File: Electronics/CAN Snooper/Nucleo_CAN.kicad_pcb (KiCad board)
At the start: 2 copper layers, 54.6 x 50.8 mm, 38 parts, among them J1 Car Power, J2 CAN Bus, SW1 Reset, T1 12V Iso Test, T10 CAN L Test, T11 CAN Output GND Test, T2 5V Iso Test, T3 9V Test, T4 3.3V Test, T5 CAN PwrSense Test, T6 CAN Tx Test, T7 CAN Rx Test, T8 CAN Input GND Test, T9 CAN H Test, U1 PDS1-S12-S9-M, U2 MCP1702T-5002E/CB, U3 Nucleo_L432KC, U4 ADM3054

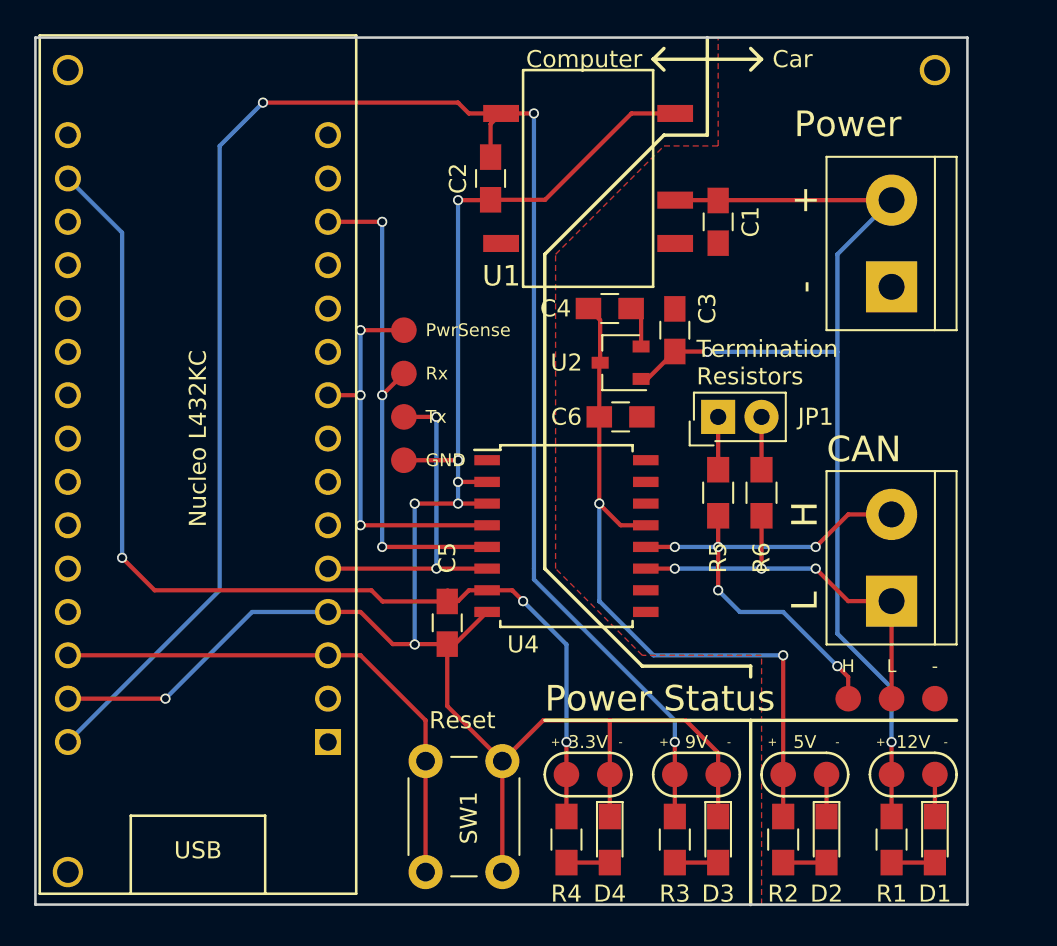
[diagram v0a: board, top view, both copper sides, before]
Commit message: CAN Snooper: PCB: Rerouted for new connectors; bumped PCB rev.
I reimported the netlist into the PCB and rerouted the car side of the
board to accommodate the new connectors. I also added a ground plane
to the computer side of the board and rerouted its traces to
accommodate said plane.
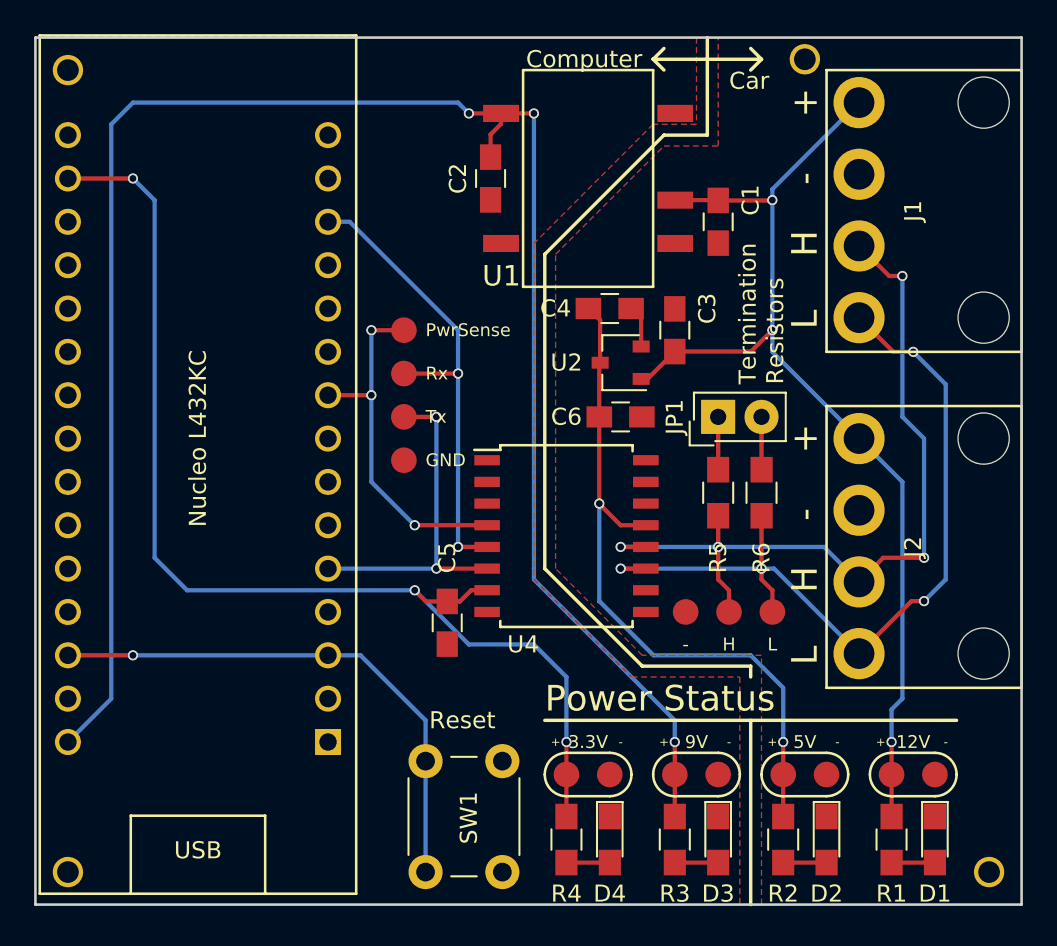
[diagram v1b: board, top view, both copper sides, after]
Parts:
- added REF**: MountingHole, Custom:MountingHole, F.Cu at (212.7, 100.3)
- J1: value Car Power -> CAN_In; footprint Connectors_Terminal_Blocks:TerminalBlock_bornier-2_P5.08mm -> Custom:Molex-MiniFitJr-4-peg
- J2: value CAN Bus -> CAN_Out; footprint Connectors_Terminal_Blocks:TerminalBlock_bornier-2_P5.08mm -> Custom:Molex-MiniFitJr-4-peg
- moved T11 15.5 mm to (194.9, 85.1)
- moved J1 11.0 mm to (205.1, 55.2), turned to 0 degrees
- moved J2 9.71 mm to (205.1, 74.9), turned to 0 degrees
- moved T10 8.64 mm to (200.0, 85.1)
- moved T9 8.64 mm to (197.5, 85.1)
- moved REF** 7.65 mm to (201.9, 52.7)
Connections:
- J1 pad 1: GNDPWR -> +12V
- J1 pad 2: +12V -> GNDPWR
- J2 pad 1: /CAN_L -> +12V
- J2 pad 2: /CAN_H -> GNDPWR
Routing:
- net GND: track 116.7 -> 0.00 mm, vias 7 -> 0
- net /CAN_L: track 24.0 -> 48.4 mm, vias 3 -> 4
- net /CAN_H: track 30.5 -> 46.9 mm, vias 5 -> 4
- net GNDPWR: track 7.39 -> 2.47 mm
- net +9V: track 105.8 -> 110.2 mm
- net +3V3: track 63.0 -> 66.5 mm
- net /CAN_Rx: track 30.2 -> 27.8 mm, vias 3 -> 2
- net /CAN_PwrSense: track 23.3 -> 21.2 mm
- net +12V: track 63.6 -> 62.0 mm, vias 2 -> 3
- net +5VP: track 42.3 -> 41.2 mm
- net /RST: track 31.9 -> 31.4 mm, vias 0 -> 1
- added copper zone on F.Cu, net GND
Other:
- board size 54.6 x 50.8 mm -> 57.8 x 50.8 mm
- board text removed: "CAN"
- board text removed: "Power"

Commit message: CAN Snooper: PCB: Use nonplated M2 screw mounting holes
The previous mounting holes were a nonstandard size as far as I could
tell, so I replaced them with properly sized holes for M2 screws. I
also added circles in the Dwgs.User layer to indicate estimated screw
head size.

The components on the PCB may need to be moved around to make sure the
screw heads fit completely onto the PCB unobstructed.

Added three new footprints for mounting holes for metric screw sizes
M1.6, M1.8, and M2. Removed the old mounting hole footprint.
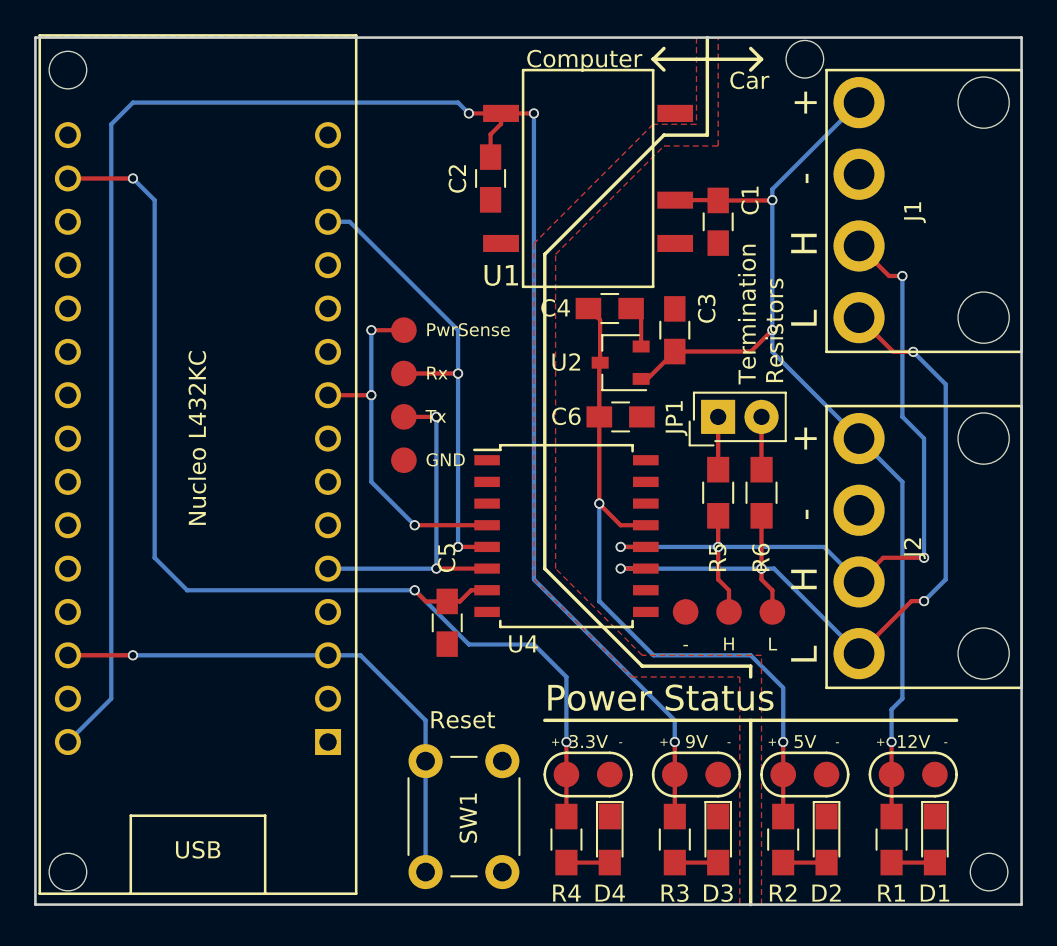
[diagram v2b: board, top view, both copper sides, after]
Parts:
- REF** (x4): footprint Custom:MountingHole -> Custom:MountingHole-M2-nonplated
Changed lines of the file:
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@@
     (links 71)
     (no_connects 0)
-    (area 156.769999 51.359999 211.530001 102.310001)
+    (area 148.689287 47.465 219.280001 104.077381)
     (thickness 1.6)
-    (drawings 53)
+    (drawings 57)
     (tracks 156)
     (zones 0)
@@
     (pad "" np_thru_hole circle (at 7.3 0) (size 3 3) (drill 3) (layers *.Cu))
   )
-  (module Custom:MountingHole (layer F.Cu)
-    (at 212.725 100.33)
-    (fp_text reference REF** (at 0 2.54) (layer F.SilkS) hide
-      (effects (font (size 1 1) (thickness 0.15)))
-    )
-    (fp_text value MountingHole (at 0 -2.54) (layer F.Fab)
-      (effects (font (size 1 1) (thickness 0.15)))
-    )
-    (pad "" thru_hole circle (at 0 0) (size 1.778 1.778) (drill 1.27) (layers *.Cu *.Mask))
-  )
   (module Connectors_Samtec:SL-102-X-XX_1x02 (layer F.Cu)
     (at 196.85 73.66 90)
@@
       (net 6 +3V3) (zone_connect 2))
   )
-  (module Custom:MountingHole (layer F.Cu)
-    (at 158.75 53.34)
-    (fp_text reference REF** (at 0 2.54) (layer F.SilkS) hide
-      (effects (font (size 1 1) (thickness 0.15)))
-    )
-    (fp_text value MountingHole (at 0 -2.54) (layer F.Fab)
-      (effects (font (size 1 1) (thickness 0.15)))
-    )
-    (pad "" thru_hole circle (at 0 0) (size 1.778 1.778) (drill 1.27) (layers *.Cu *.Mask))
-  )
-  (module Custom:MountingHole (layer F.Cu)
-    (at 158.75 100.33)
-    (fp_text reference REF** (at 0 2.54) (layer F.SilkS) hide
-      (effects (font (size 1 1) (thickness 0.15)))
-    )
-    (fp_text value MountingHole (at 0 -2.54) (layer F.Fab)
-      (effects (font (size 1 1) (thickness 0.15)))
-    )
-    (pad "" thru_hole circle (at 0 0) (size 1.778 1.778) (drill 1.27) (layers *.Cu *.Mask))
-  )
-  (module Custom:MountingHole (layer F.Cu)
-    (at 201.93 52.705)
-    (fp_text reference REF** (at 0 2.54) (layer F.SilkS) hide
-      (effects (font (size 1 1) (thickness 0.15)))
-    )
-    (fp_text value MountingHole (at 0 -2.54) (layer F.Fab)
-      (effects (font (size 1 1) (thickness 0.15)))
-    )
-    (pad "" thru_hole circle (at 0 0) (size 1.778 1.778) (drill 1.27) (layers *.Cu *.Mask))
-  )
   (module Custom:Molex-MiniFitJr-4-peg (layer F.Cu)
     (at 205.105 55.245)
@@
     (pad "" np_thru_hole circle (at 7.3 0) (size 3 3) (drill 3) (layers *.Cu))
   )
+  (module Custom:MountingHole-M2-nonplated (layer F.Cu)
+    (at 158.75 53.34)
+    (fp_text reference REF** (at 0 1.905) (layer F.SilkS) hide
+      (effects (font (size 1 1) (thickness 0.15)))
+    )
+    (fp_text value MountingHole (at 0 -1.905) (layer F.Fab)
+      (effects (font (size 1 1) (thickness 0.15)))
+    )
+    (pad "" np_thru_hole circle (at 0 0) (size 2.2 2.2) (drill 2.2) (layers *.Cu *.Mask))
+  )
+  (module Custom:MountingHole-M2-nonplated (layer F.Cu)
+    (at 158.75 100.33)
+    (fp_text reference REF** (at 0 1.905) (layer F.SilkS) hide
+      (effects (font (size 1 1) (thickness 0.15)))
+    )
+    (fp_text value MountingHole (at 0 -1.905) (layer F.Fab)
+      (effects (font (size 1 1) (thickness 0.15)))
+    )
+    (pad "" np_thru_hole circle (at 0 0) (size 2.2 2.2) (drill 2.2) (layers *.Cu *.Mask))
+  )
+  (module Custom:MountingHole-M2-nonplated (layer F.Cu)
+    (at 212.725 100.33)
+    (fp_text reference REF** (at 0 1.905) (layer F.SilkS) hide
+      (effects (font (size 1 1) (thickness 0.15)))
+    )
+    (fp_text value MountingHole (at 0 -1.905) (layer F.Fab)
+      (effects (font (size 1 1) (thickness 0.15)))
+    )
+    (pad "" np_thru_hole circle (at 0 0) (size 2.2 2.2) (drill 2.2) (layers *.Cu *.Mask))
+  )
+  (module Custom:MountingHole-M2-nonplated (layer F.Cu)
+    (at 201.93 52.705)
+    (fp_text reference REF** (at 0 1.905) (layer F.SilkS) hide
+      (effects (font (size 1 1) (thickness 0.15)))
+    )
+    (fp_text value MountingHole (at 0 -1.905) (layer F.Fab)
+      (effects (font (size 1 1) (thickness 0.15)))
+    )
+    (pad "" np_thru_hole circle (at 0 0) (size 2.2 2.2) (drill 2.2) (layers *.Cu *.Mask))
+  )
+  (gr_circle (center 201.93 52.705) (end 201.93 54.905) (layer Dwgs.User) (width 0.2))
+  (gr_circle (center 212.725 100.33) (end 212.725 102.53) (layer Dwgs.User) (width 0.2))
+  (gr_circle (center 158.75 100.33) (end 158.75 102.53) (layer Dwgs.User) (width 0.2))
+  (gr_circle (center 158.75 53.34) (end 158.75 55.54) (layer Dwgs.User) (width 0.2))
   (dimension 57.785 (width 0.3) (layer Eco1.User)
     (gr_text "2.2750 in" (at 185.7375 48.815) (layer Eco1.User)
